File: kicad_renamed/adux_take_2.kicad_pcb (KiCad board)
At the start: 2 copper layers, 137.7 x 118.5 mm, 36 parts

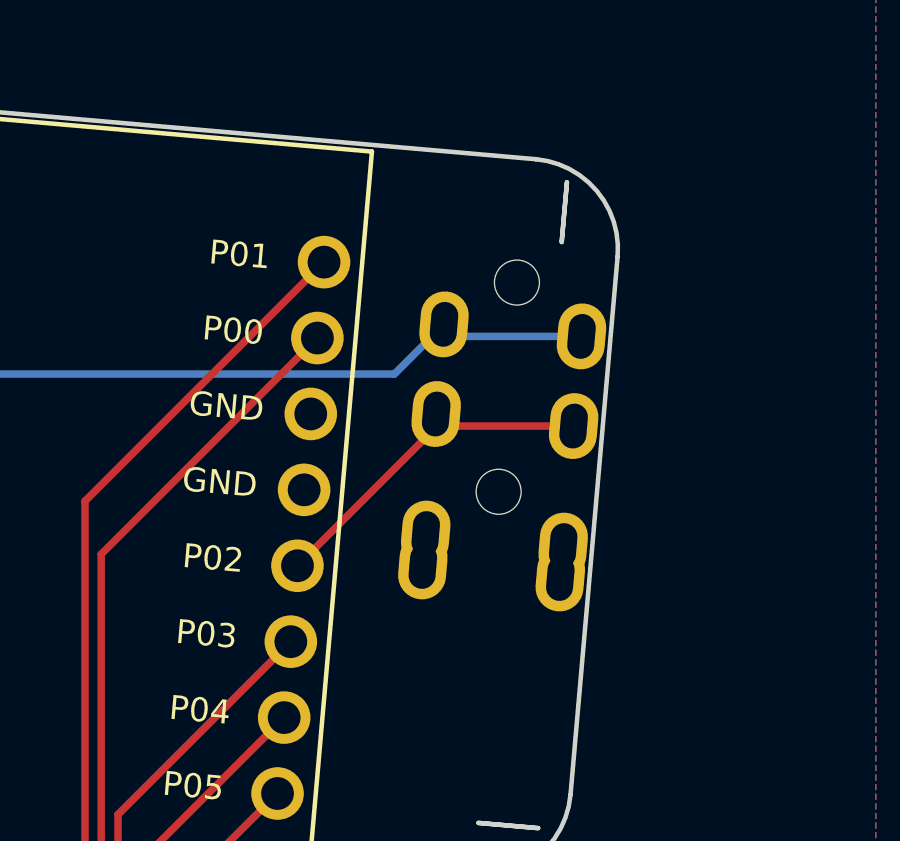
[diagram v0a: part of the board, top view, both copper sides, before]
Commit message: Updated pcb and project files
Part of the trrs jack change
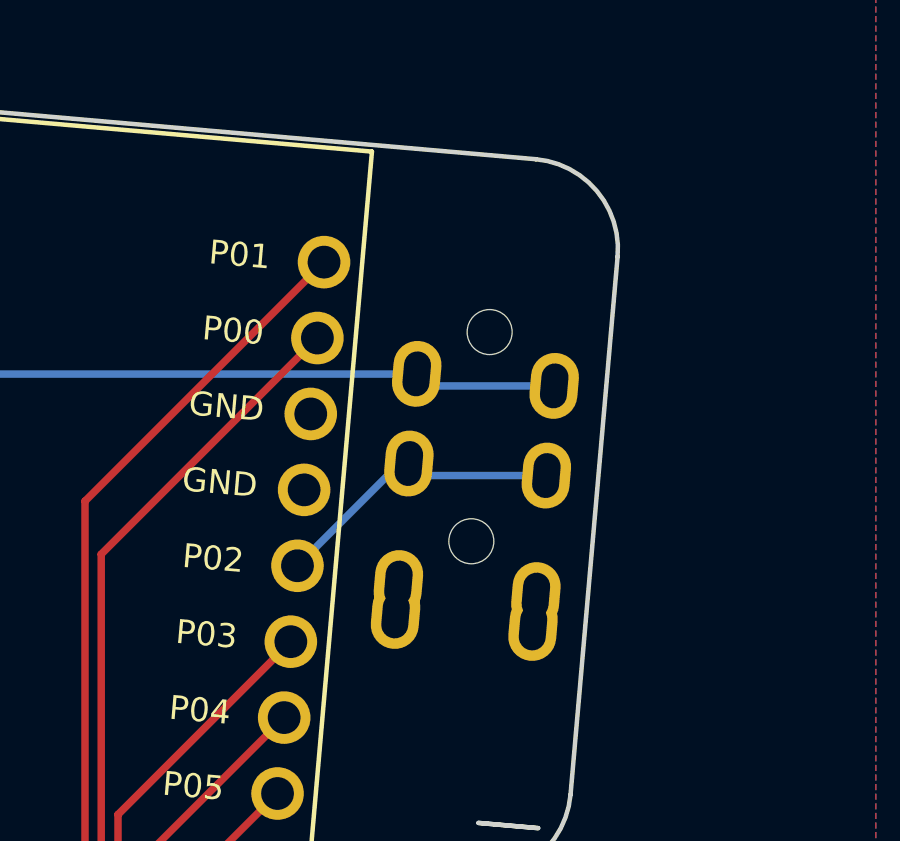
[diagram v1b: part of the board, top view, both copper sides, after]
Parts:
- moved REF** 1.88 mm to (127.1, -46.2)
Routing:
- net VCC: track 26.3 -> 24.0 mm
- net P2: track 11.7 -> 9.87 mm
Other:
- outline, holes or cut-outs redrawn
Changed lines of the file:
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@@
       (outputformat 1)
       (mirror false)
-      (drillshape 1)
+      (drillshape 0)
       (scaleselection 1)
-      (outputdirectory "")
+      (outputdirectory "gerbers/")
     )
   )
@@
   )
   (footprint "TRRS-PJ-320A-dual" (layer "F.Cu")
-    (at 128.00854 -47.801987 -5)
+    (at 127.09854 -46.151987 -5)
     (attr through_hole)
     (fp_text reference "REF**" (at 0 14.2) (layer "Dwgs.User")
@@
   (gr_arc (start 85.976294 -73.162976) (mid 85.297405 -73.516383) (end 85.067255 -74.246327) (layer "Edge.Cuts") (width 0.15))
   (gr_arc (start 127.364277 -29.339013) (mid 126.304056 -27.302347) (end 124.114226 -26.611896) (layer "Edge.Cuts") (width 0.15))
-  (gr_arc (start 127.244312 -49.752388) (mid 127.07 -47.76) (end 127.244312 -49.752388) (layer "Edge.Cuts") (width 0.15))
   (gr_line (start 26.106344 8.616255) (end 25.647422 6.903534) (layer "Edge.Cuts") (width 0.15))
   (gr_arc (start 120.989154 14.714985) (mid 121.45508 15.322192) (end 121.35518 16.081011) (layer "Edge.Cuts") (width 0.15))
@@
   (segment (start 101.157858 22.439337) (end 102.455221 23.7367) (width 0.25) (layer "B.Cu") (net 18))
   (segment (start 102.329136 14.865086) (end 101.157858 16.036364) (width 0.25) (layer "B.Cu") (net 18))
-  (segment (start 123.147146 -45.01508) (end 121.490742 -43.358676) (width 0.25) (layer "B.Cu") (net 21))
-  (segment (start 123.548062 -44.614164) (end 123.147146 -45.01508) (width 0.25) (layer "B.Cu") (net 21))
+  (segment (start 122.638062 -42.964164) (end 122.237146 -43.36508) (width 0.25) (layer "B.Cu") (net 21))
+  (segment (start 126.819642 -42.964164) (end 122.638062 -42.964164) (width 0.25) (layer "B.Cu") (net 21))
   (segment (start 121.490742 -43.358676) (end 105.833352 -43.358676) (width 0.25) (layer "B.Cu") (net 21))
   (segment (start 105.833352 -43.358676) (end 103.301747 -40.827071) (width 0.25) (layer "B.Cu") (net 21))
-  (segment (start 127.729642 -44.614164) (end 123.548062 -44.614164) (width 0.25) (layer "B.Cu") (net 21))
-  (segment (start 123.286595 -41.62558) (end 122.885679 -42.026496) (width 0.25) (layer "F.Cu") (net 22))
-  (segment (start 127.468174 -41.62558) (end 123.286595 -41.62558) (width 0.25) (layer "F.Cu") (net 22))
-  (segment (start 122.885679 -41.591783) (end 118.262379 -36.968483) (width 0.25) (layer "F.Cu") (net 22))
-  (segment (start 122.885679 -42.026496) (end 122.885679 -41.591783) (width 0.25) (layer "F.Cu") (net 22))
+  (segment (start 121.670392 -40.376496) (end 118.262379 -36.968483) (width 0.25) (layer "B.Cu") (net 22))
+  (segment (start 122.376595 -39.97558) (end 121.975679 -40.376496) (width 0.25) (layer "B.Cu") (net 22))
+  (segment (start 126.558174 -39.97558) (end 122.376595 -39.97558) (width 0.25) (layer "B.Cu") (net 22))
+  (segment (start 121.975679 -40.376496) (end 121.670392 -40.376496) (width 0.25) (layer "B.Cu") (net 22))
   (zone (net 2) (net_name "GND") (layers F&B.Cu) (hatch edge 0.508)
     (connect_pads (clearance 0.508))
